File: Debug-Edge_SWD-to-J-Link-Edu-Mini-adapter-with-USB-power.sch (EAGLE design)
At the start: 8 parts, among them J1 AVX_6-PIN_009159006061916, J3 CORTEX_DEBUG_SMD, J4 10118194-0001LF, U1 MIC5504-3.3YM5-TR

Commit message: Updated README. Added PCB images.
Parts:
- FRAME1: value FRAME-LETTER -> FRAME-LETTERNO_PACKAGE; device SparkFun-Aesthetics:FRAME-LETTER -> SparkFun-Aesthetics:FRAME-LETTERNO_PACKAGE; DESIGNER (none) -> Nathan Jones
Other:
- note removed: "Nathan Jones"
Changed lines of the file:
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@@
 </classes>
 <parts>
-<part name="FRAME1" library="SparkFun-Aesthetics" deviceset="FRAME-LETTER" device=""/>
 <part name="GND1" library="SparkFun-PowerSymbols" deviceset="GND" device=""/>
 <part name="C1" library="adafruit" deviceset="C-US" device="C0805" value="1uF"/>
@@
 <part name="J3" library="SparkFun-Connectors" deviceset="CORTEX_DEBUG" device="_SMD"/>
 <part name="U1" library="MIC5504-3.3YM5-TR" deviceset="MIC5504-3.3YM5-TR" device=""/>
+<part name="FRAME1" library="SparkFun-Aesthetics" deviceset="FRAME-LETTER" device="NO_PACKAGE">
+<attribute name="DESIGNER" value="Nathan Jones"/>
+</part>
 </parts>
 <sheets>
 <sheet>
 <plain>
-<text x="167.64" y="7.62" size="5.08" layer="94" ratio="6">Nathan Jones</text>
 </plain>
 <instances>
-<instance part="FRAME1" gate="G$1" x="0" y="0" smashed="yes"/>
-<instance part="FRAME1" gate="V" x="147.32" y="0" smashed="yes">
-<attribute name="LAST_DATE_TIME" x="160.02" y="1.27" size="2.54" layer="94" font="vector"/>
-<attribute name="SHEET" x="233.68" y="1.27" size="2.54" layer="94" font="vector"/>
-<attribute name="DRAWING_NAME" x="162.814" y="17.78" size="2.7432" layer="94" font="vector"/>
-<attribute name="DESIGNER" x="170.434" y="11.176" size="2.7432" layer="94" font="vector"/>
-<attribute name="REV" x="236.22" y="6.604" size="2.7432" layer="94" font="vector"/>
-</instance>
 <instance part="GND1" gate="1" x="177.8" y="86.36" smashed="yes">
 <attribute name="VALUE" x="177.8" y="86.106" size="1.778" layer="96" align="top-center"/>
@@
 <attribute name="VALUE" x="157.7594" y="113.2586" size="2.0828" layer="96" ratio="6" rot="SMR0"/>
 </instance>
+<instance part="FRAME1" gate="G$1" x="0" y="0" smashed="yes"/>
+<instance part="FRAME1" gate="V" x="147.32" y="0" smashed="yes">
+<attribute name="LAST_DATE_TIME" x="160.02" y="1.27" size="2.54" layer="94" font="vector"/>
+<attribute name="SHEET" x="233.68" y="1.27" size="2.54" layer="94" font="vector"/>
+<attribute name="DRAWING_NAME" x="162.814" y="17.78" size="2.7432" layer="94" font="vector"/>
+<attribute name="DESIGNER" x="170.434" y="11.176" size="2.7432" layer="94" font="vector"/>
+</instance>
 </instances>

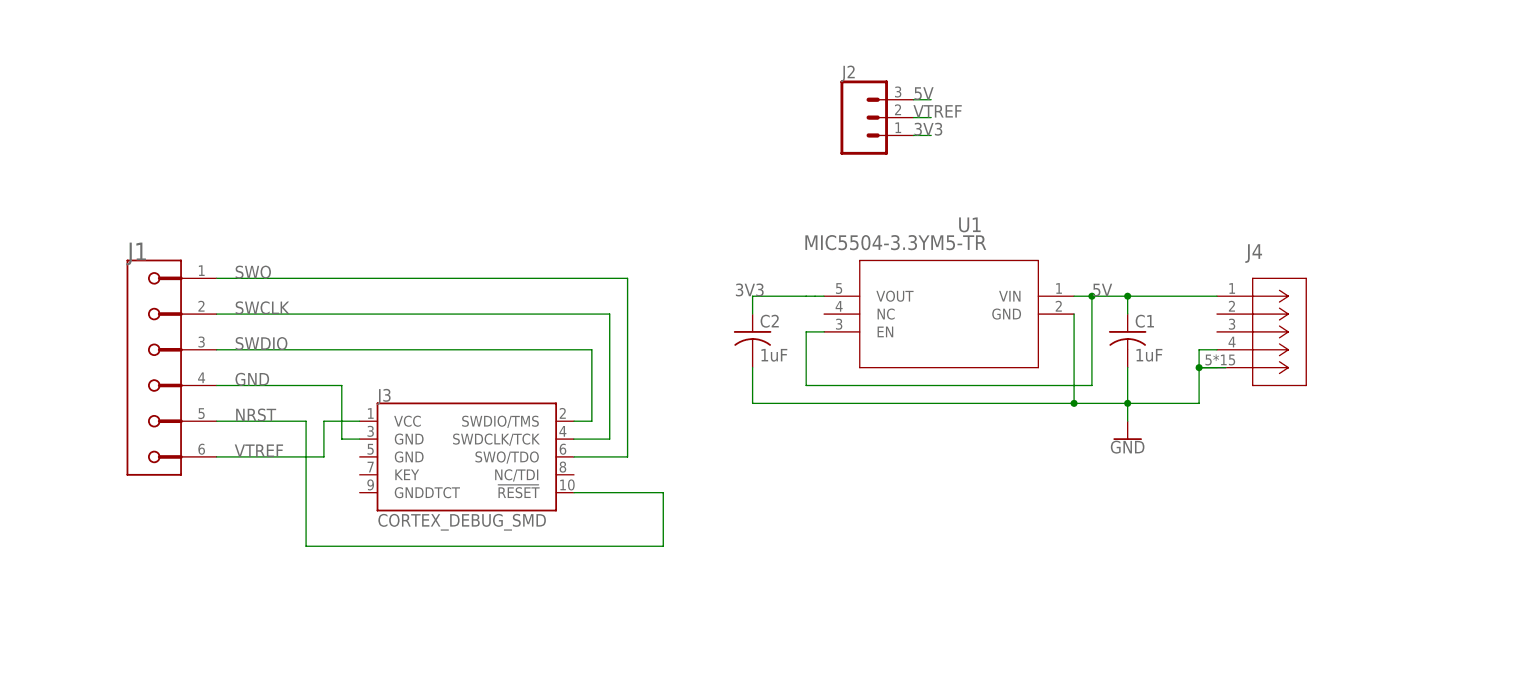
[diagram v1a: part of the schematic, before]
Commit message: Updated AVX library. Changed to PTH components.
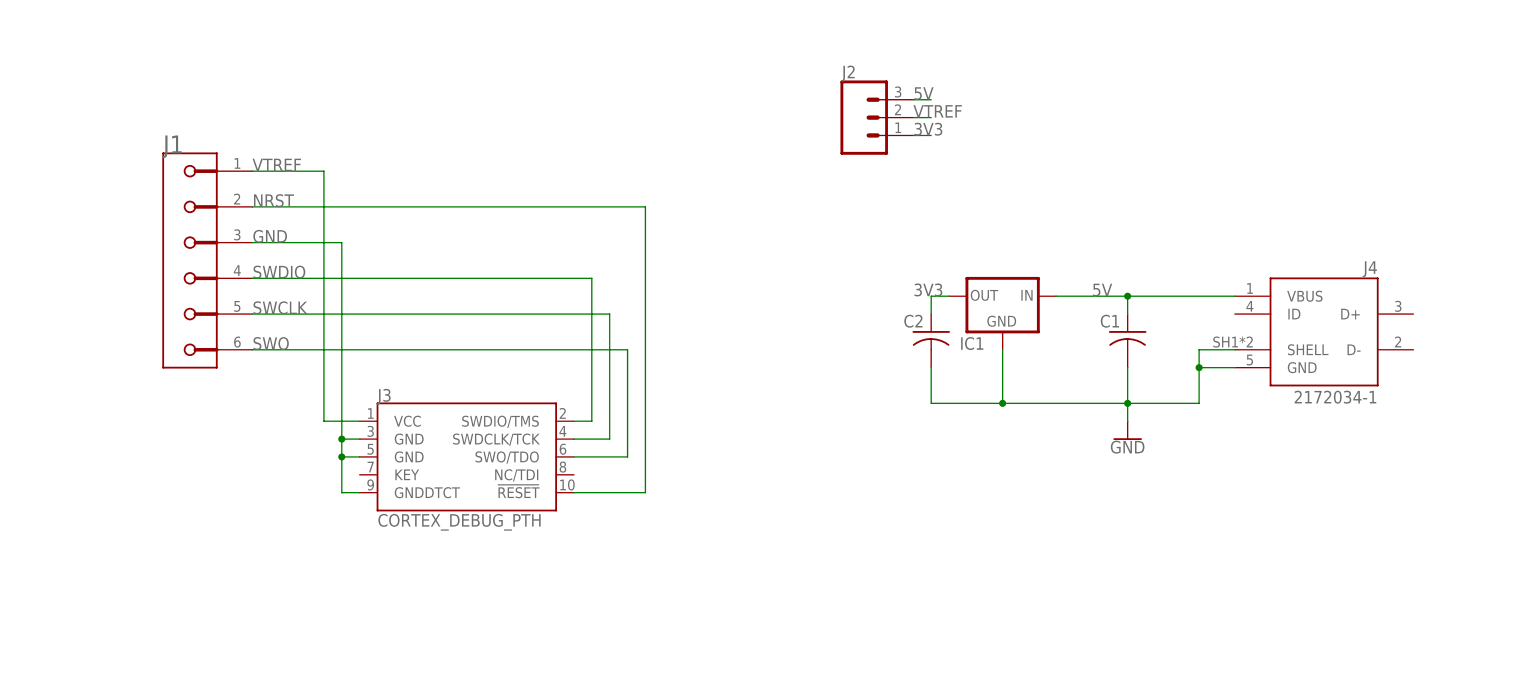
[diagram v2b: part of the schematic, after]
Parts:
- removed U1: MIC5504-3.3YM5-TR, MIC5504-3.3YM5-TR:MIC5504-3.3YM5-TR
- added IC1: (no value), adafruit:MCP1700INLINE
- C1, C2: value 1uF -> (none); device adafruit:C-USC0805 -> adafruit:C-US025-024X044
- J3: value CORTEX_DEBUG_SMD -> CORTEX_DEBUG_PTH; device SparkFun-Connectors:CORTEX_DEBUG_SMD -> SparkFun-Connectors:CORTEX_DEBUG_PTH
- J4: value 10118194-0001LF -> 2172034-1; device USB-micro-B_Amphenol_10118194-0001LF:10118194-0001LF -> USB-mini-B_TE_2172034-1:2172034-1
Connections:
- net 3V3: now also IC1.OUT; no longer U1.VOUT
- net 5V: now also IC1.IN, J4.VBUS; no longer J4.1, U1.EN, U1.VIN
- net GND: now also IC1.GND, J1.3, J3.GND@5, J3.GNDDTCT, J4.GND, J4.SHELL; no longer J1.4, J4.4, J4.5, U1.GND
- net NRST: now also J1.2; no longer J1.5
- net SWCLK: now also J1.5; no longer J1.2
- net SWDIO: now also J1.4; no longer J1.3
- net SWO: now also J1.6; no longer J1.1
- net VTREF: now also J1.1; no longer J1.6
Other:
- moved on the sheet: C2, J1

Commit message: Updated footprint for USB connector.
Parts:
- removed J4: 2172034-1, USB-mini-B_TE_2172034-1:2172034-1
- added J5: 2172034-1, 2172034-1:2172034-1
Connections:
- net 5V: now also J5.1; no longer J4.VBUS
- net GND: now also J5.4, J5.5, J5.MH1, J5.MH2; no longer J4.GND, J4.SHELL
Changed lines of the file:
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@@
 </part>
 <part name="J3" library="SparkFun-Connectors" deviceset="CORTEX_DEBUG" device="_PTH"/>
-<part name="J4" library="USB-mini-B_TE_2172034-1" deviceset="2172034-1" device=""/>
 <part name="IC1" library="adafruit" deviceset="MCP1700" device="INLINE"/>
 <part name="C1" library="adafruit" deviceset="C-US" device="025-024X044"/>
 <part name="C2" library="adafruit" deviceset="C-US" device="025-024X044"/>
+<part name="J5" library="2172034-1" deviceset="2172034-1" device=""/>
 </parts>
 <sheets>
@@
 <attribute name="VALUE" x="71.12" y="73.914" size="1.778" layer="96" font="vector"/>
 </instance>
-<instance part="J4" gate="G$1" x="205.74" y="101.6" smashed="yes" rot="MR0">
-<attribute name="NAME" x="213.368590625" y="109.8643" size="1.78" layer="95" rot="MR0"/>
-<attribute name="VALUE" x="213.36643125" y="91.4314" size="1.7795" layer="96" rot="MR0"/>
-</instance>
 <instance part="IC1" gate="1" x="160.02" y="106.68" smashed="yes" rot="MR0">
 <attribute name="NAME" x="157.48" y="99.06" size="1.778" layer="95" rot="MR0"/>
@@
 <attribute name="VALUE" x="148.844" y="97.409" size="1.778" layer="96" rot="MR0"/>
 </instance>
+<instance part="J5" gate="G$1" x="193.04" y="106.68" smashed="yes">
+<attribute name="NAME" x="212.09" y="114.3" size="1.778" layer="95" align="center-left"/>
+<attribute name="VALUE" x="212.09" y="111.76" size="1.778" layer="96" align="center-left"/>
+</instance>
 </instances>
 <busses>
@@
 <pinref part="GND1" gate="1" pin="GND"/>
 <wire x1="177.8" y1="91.44" x2="177.8" y2="88.9" width="0.1524" layer="91"/>
-<wire x1="187.96" y1="99.06" x2="187.96" y2="96.52" width="0.1524" layer="91"/>
-<wire x1="187.96" y1="96.52" x2="187.96" y2="91.44" width="0.1524" layer="91"/>
-<junction x="187.96" y="96.52"/>
+<wire x1="187.96" y1="99.06" x2="187.96" y2="91.44" width="0.1524" layer="91"/>
 <wire x1="177.8" y1="96.52" x2="177.8" y2="91.44" width="0.1524" layer="91"/>
 <wire x1="177.8" y1="91.44" x2="187.96" y2="91.44" width="0.1524" layer="91"/>
@@
 <wire x1="149.86" y1="91.44" x2="160.02" y2="91.44" width="0.1524" layer="91"/>
 <wire x1="160.02" y1="91.44" x2="177.8" y2="91.44" width="0.1524" layer="91"/>
-<wire x1="193.04" y1="96.52" x2="187.96" y2="96.52" width="0.1524" layer="91"/>
 <pinref part="C1" gate="G$1" pin="2"/>
-<pinref part="J4" gate="G$1" pin="GND"/>
-<pinref part="J4" gate="G$1" pin="SHELL"/>
 <wire x1="193.04" y1="99.06" x2="187.96" y2="99.06" width="0.1524" layer="91"/>
 <pinref part="IC1" gate="1" pin="GND"/>
@@
 <pinref part="C2" gate="G$1" pin="2"/>
 <wire x1="149.86" y1="96.52" x2="149.86" y2="91.44" width="0.1524" layer="91"/>
+<pinref part="J5" gate="G$1" pin="4"/>
+<wire x1="187.96" y1="91.44" x2="218.44" y2="91.44" width="0.1524" layer="91"/>
+<junction x="187.96" y="91.44"/>
+<wire x1="218.44" y1="91.44" x2="218.44" y2="101.6" width="0.1524" layer="91"/>
+<pinref part="J5" gate="G$1" pin="5"/>
+<wire x1="218.44" y1="101.6" x2="218.44" y2="104.14" width="0.1524" layer="91"/>
+<wire x1="218.44" y1="104.14" x2="218.44" y2="106.68" width="0.1524" layer="91"/>
+<wire x1="218.44" y1="106.68" x2="215.9" y2="106.68" width="0.1524" layer="91"/>
+<pinref part="J5" gate="G$1" pin="MH1"/>
+<wire x1="215.9" y1="104.14" x2="218.44" y2="104.14" width="0.1524" layer="91"/>
+<junction x="218.44" y="104.14"/>
+<pinref part="J5" gate="G$1" pin="MH2"/>
+<wire x1="215.9" y1="101.6" x2="218.44" y2="101.6" width="0.1524" layer="91"/>
+<junction x="218.44" y="101.6"/>
 </segment>
 <segment>
@@
 <label x="172.72" y="106.68" size="1.778" layer="95"/>
 <pinref part="C1" gate="G$1" pin="1"/>
-<pinref part="J4" gate="G$1" pin="VBUS"/>
 <pinref part="IC1" gate="1" pin="IN"/>
 <wire x1="177.8" y1="106.68" x2="167.64" y2="106.68" width="0.1524" layer="91"/>
+<pinref part="J5" gate="G$1" pin="1"/>
 </segment>
 <segment>
